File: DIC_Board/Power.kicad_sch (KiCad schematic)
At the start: 47 parts, among them Q100 CSD18542KTTT, Q101 CSD18542KTTT, U10 TPS552882RPMR, U11 TPSM53603RDAR

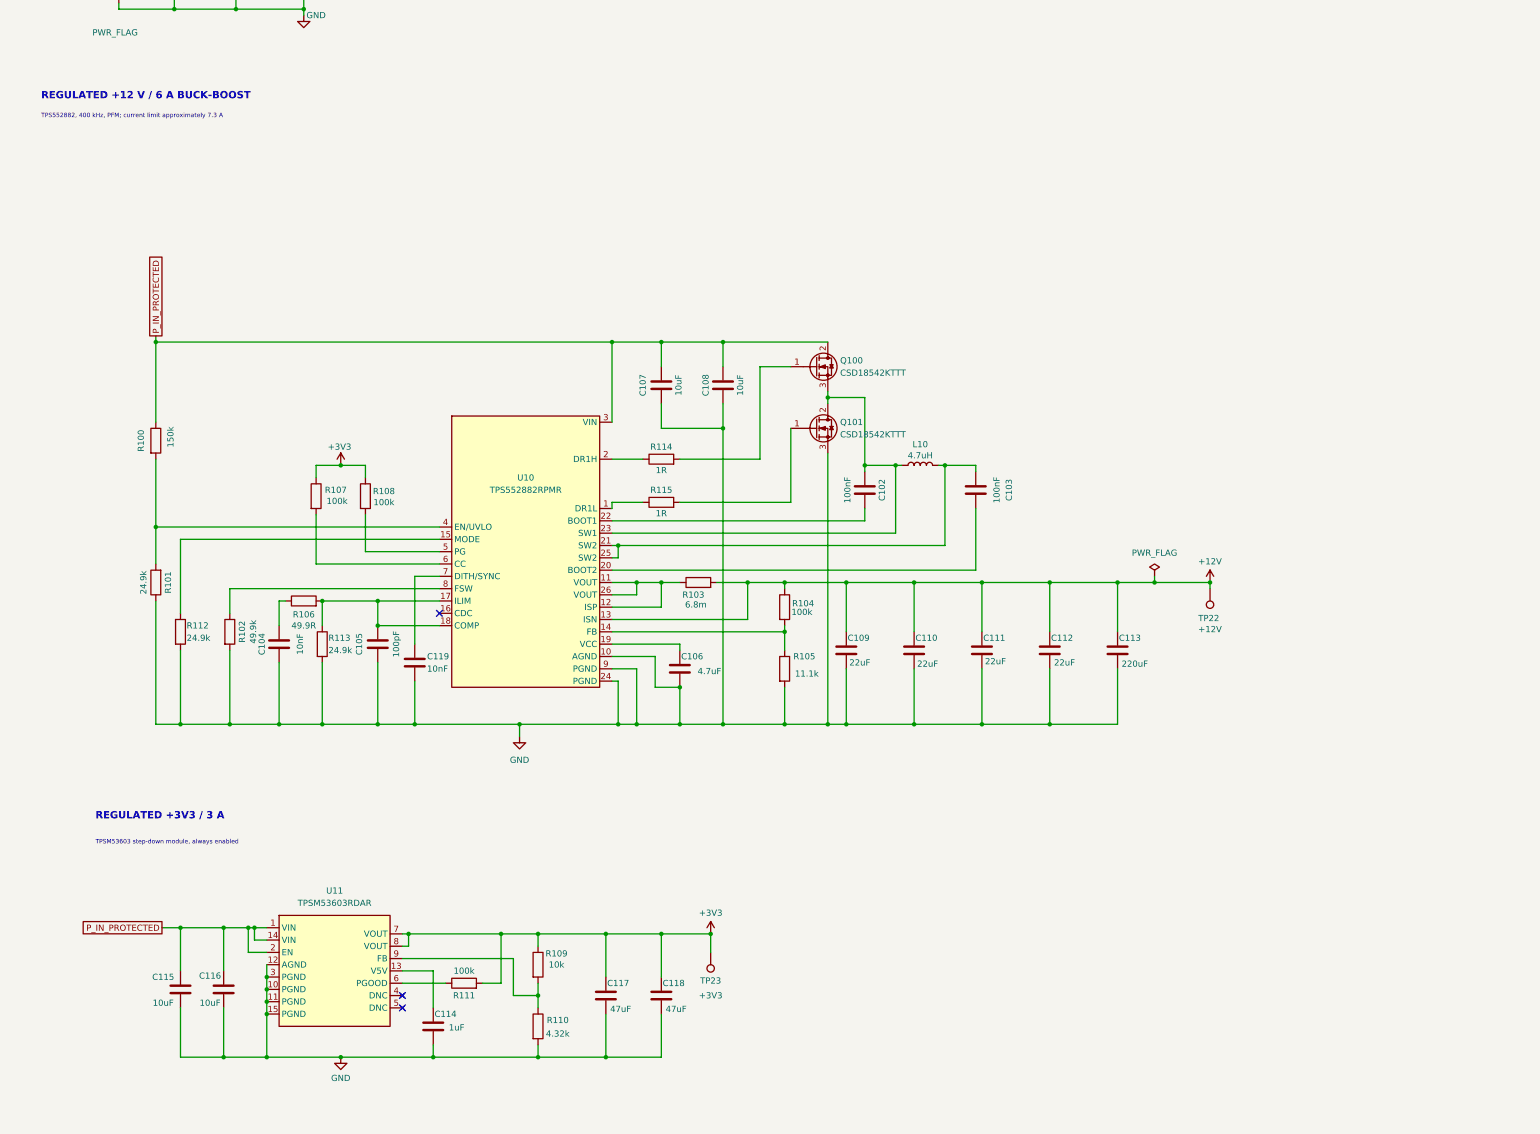
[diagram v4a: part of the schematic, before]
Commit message: added 5V and 6V power rails
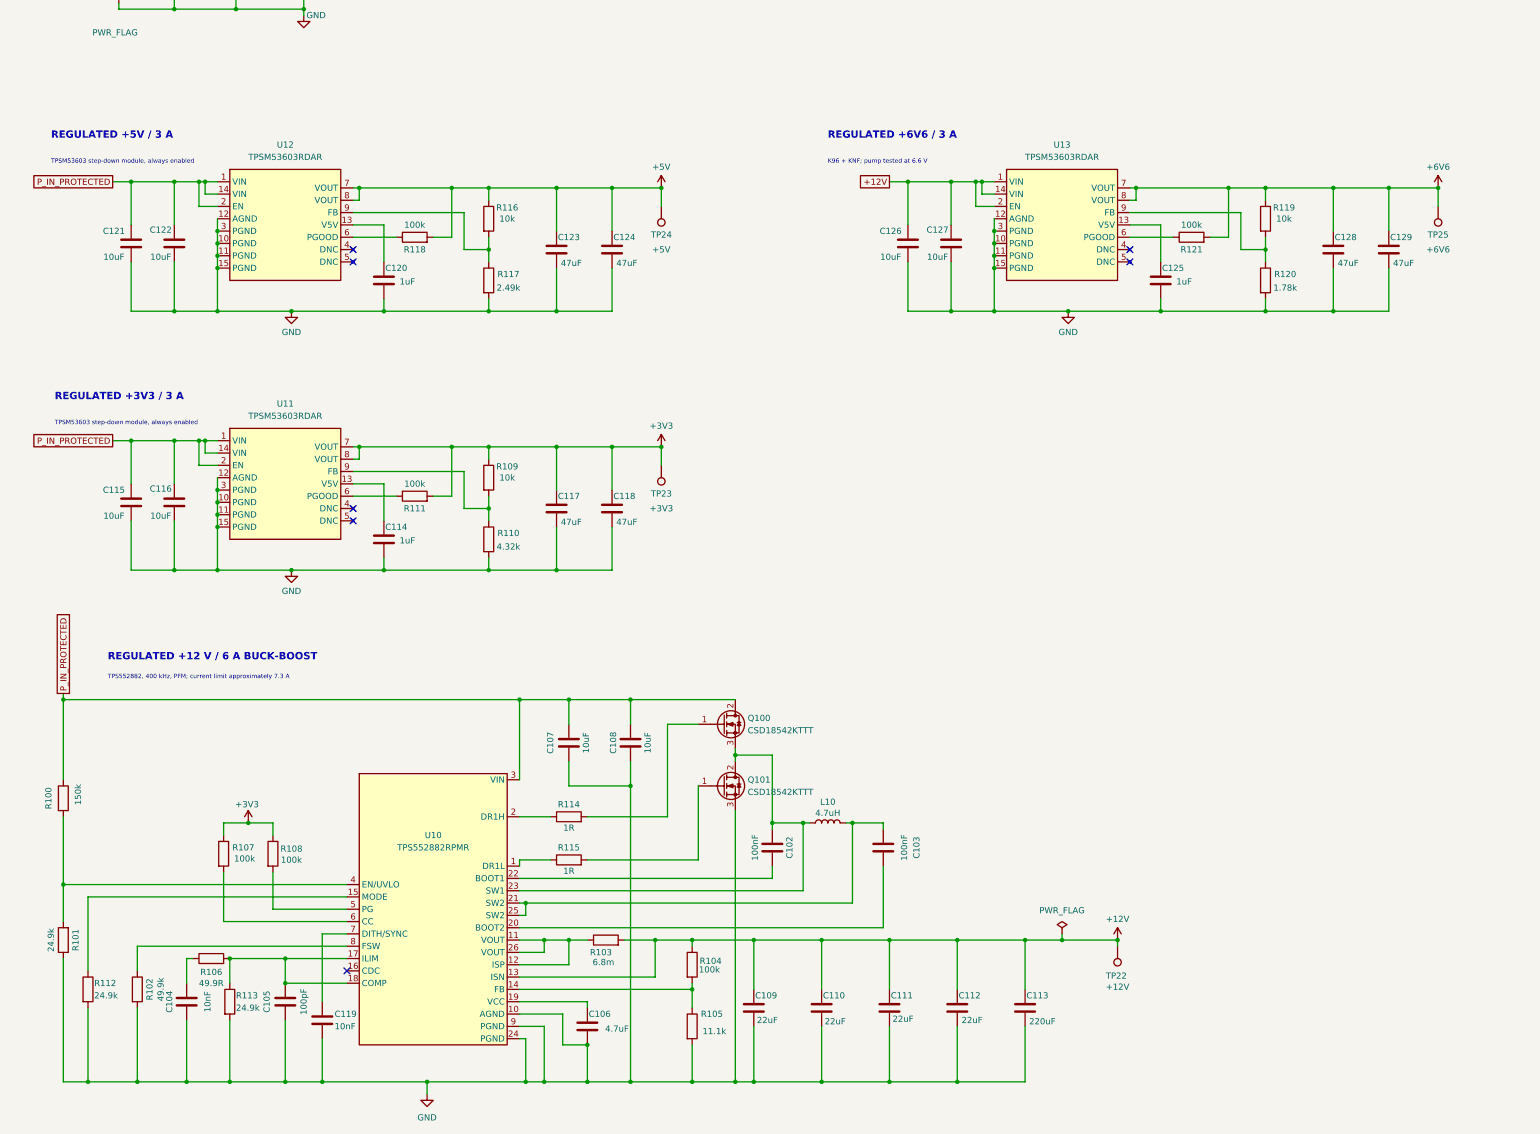
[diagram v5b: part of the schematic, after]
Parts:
- added C120, C125: 1uF, Capacitor_SMD:C_0603_1608Metric, symbol Device:C
- added C121, C122, C126, C127: 10uF, Capacitor_SMD:C_1206_3216Metric, symbol Device:C
- added C123, C124, C128, C129: 47uF, Capacitor_SMD:C_1210_3225Metric, symbol Device:C
- added R116, R119: 10k, Resistor_SMD:R_0402_1005Metric, symbol Device:R
- added R117: 2.49k, Resistor_SMD:R_0402_1005Metric, symbol Device:R
- added R118, R121: 100k, Resistor_SMD:R_0402_1005Metric, symbol Device:R
- added R120: 1.78k, Resistor_SMD:R_0402_1005Metric, symbol Device:R
- added TP24: +5V, TestPoint:TestPoint_Plated_Hole_D2.0mm, symbol Connector:TestPoint
- added TP25: +6V6, TestPoint:TestPoint_Plated_Hole_D2.0mm, symbol Connector:TestPoint
- added U12, U13: TPSM53603RDAR, Package_DFN_QFN:Texas_B3QFN-14-1EP_5x5.5mm_P0.65mm_ThermalVia, symbol DIC_Board:TPSM53603RDA
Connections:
- net +12V: now also C126.1, C127.1, U13.1 (VIN), U13.14 (VIN), U13.2 (EN)
- net GND: now also C120.2, C121.2, C122.2, C123.2, C124.2, C125.2, C126.2, C127.2, C128.2, C129.2, R117.2, R120.2, U12.10 (PGND), U12.11 (PGND), U12.12 (AGND), U12.15 (PGND), U12.3 (PGND), U13.10 (PGND), U13.11 (PGND), U13.12 (AGND), U13.15 (PGND), U13.3 (PGND)
- net P_IN_PROTECTED: now also C121.1, C122.1, U12.1 (VIN), U12.14 (VIN), U12.2 (EN)
- new net: C125.1, U13.13 (V5V)
- new net: R121.1, U13.6 (PGOOD)
- new net: R119.2, R120.1, U13.9 (FB)
- new net: R116.2, R117.1, U12.9 (FB)
- new net: C120.1, U12.13 (V5V)
- new net: R118.1, U12.6 (PGOOD)
- new net +5V: C123.1, C124.1, R116.1, R118.2, TP24.1, U12.7 (VOUT), U12.8 (VOUT)
- new net +6V6: C128.1, C129.1, R119.1, R121.2, TP25.1, U13.7 (VOUT), U13.8 (VOUT)
- no-connect marks 3 -> 7
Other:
- note added: "K96 + KNF; pump tested at 6.6 V"
- note added: "REGULATED +5V / 3 A"
- note added: "REGULATED +6V6 / 3 A"
- moved on the sheet: C102, C103, C104, C105, C106, C107, C108, C109, C110, C111, C112, C113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

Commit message: added valve control sheet
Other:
- moved on the sheet: C102, C103, C104, C105, C106, C107, C108, C109, C110, C111, C112, C113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

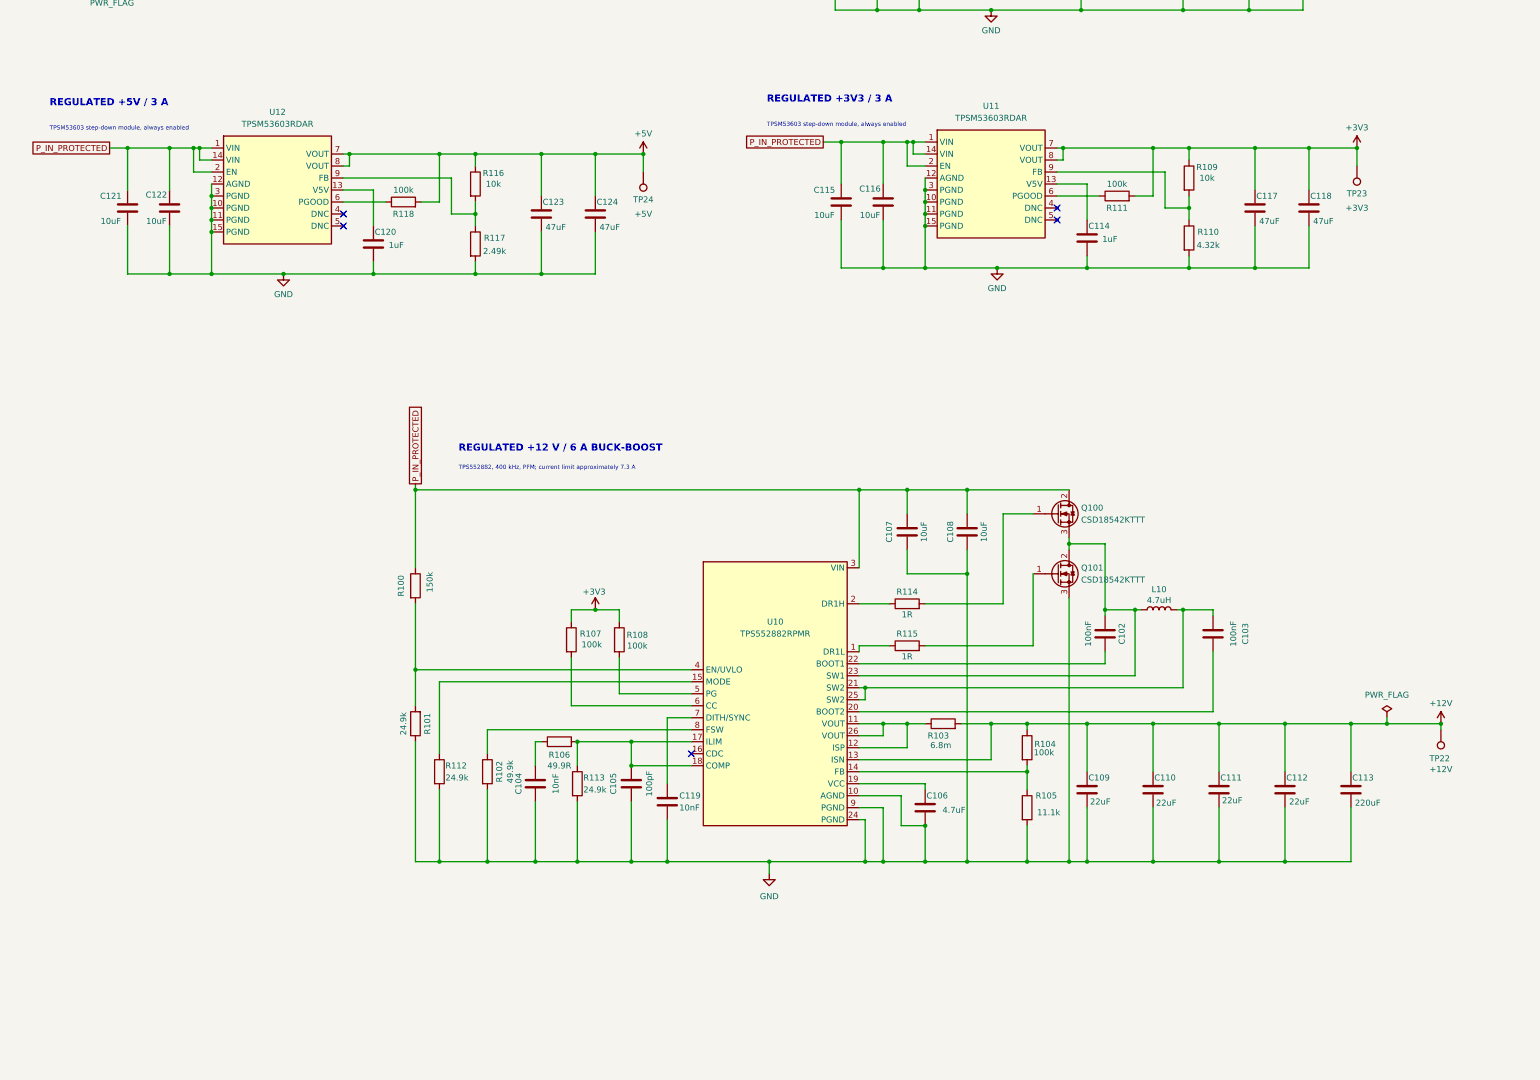
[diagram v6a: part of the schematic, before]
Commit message: Completed water pump and added the 2.7V rail
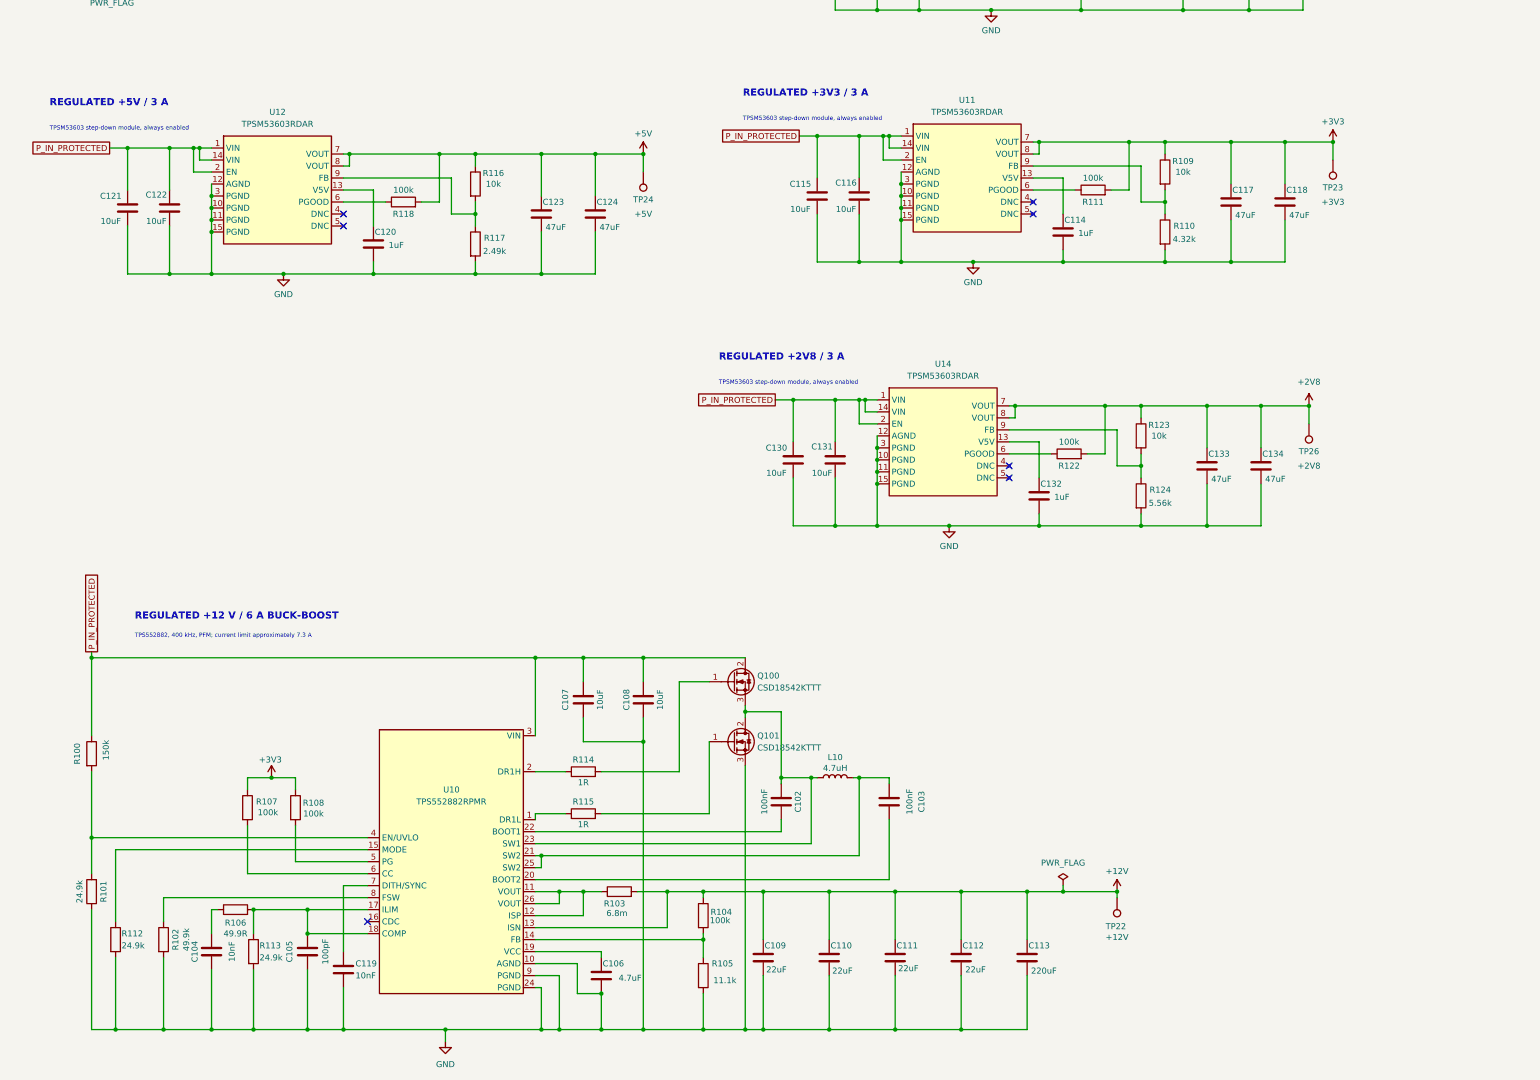
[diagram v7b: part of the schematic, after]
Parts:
- added C130, C131: 10uF, Capacitor_SMD:C_1206_3216Metric, symbol Device:C
- added C132: 1uF, Capacitor_SMD:C_0603_1608Metric, symbol Device:C
- added C133, C134: 47uF, Capacitor_SMD:C_1210_3225Metric, symbol Device:C
- added R122: 100k, Resistor_SMD:R_0402_1005Metric, symbol Device:R
- added R123: 10k, Resistor_SMD:R_0402_1005Metric, symbol Device:R
- added R124: 5.56k, Resistor_SMD:R_0402_1005Metric, symbol Device:R
- added TP26: +2V8, TestPoint:TestPoint_Plated_Hole_D2.0mm, symbol Connector:TestPoint
- added U14: TPSM53603RDAR, Package_DFN_QFN:Texas_B3QFN-14-1EP_5x5.5mm_P0.65mm_ThermalVia, symbol DIC_Board:TPSM53603RDA
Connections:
- net GND: now also C130.2, C131.2, C132.2, C133.2, C134.2, R124.2, U14.10 (PGND), U14.11 (PGND), U14.12 (AGND), U14.15 (PGND), U14.3 (PGND)
- net P_IN_PROTECTED: now also C130.1, C131.1, U14.1 (VIN), U14.14 (VIN), U14.2 (EN)
- new net: R122.1, U14.6 (PGOOD)
- new net: C132.1, U14.13 (V5V)
- new net: R123.2, R124.1, U14.9 (FB)
- new net +2V8: C133.1, C134.1, R122.2, R123.1, TP26.1, U14.7 (VOUT), U14.8 (VOUT)
- no-connect marks 7 -> 9
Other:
- note added: "REGULATED +2V8 / 3 A"
- moved on the sheet: C102, C103, C104, C105, C106, C107, C108, C109, C110, C111, C112, C113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
